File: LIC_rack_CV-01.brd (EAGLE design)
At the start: 162 x 102 mm, 53 parts, among them IC1 TS1117, IC2 MEGA32-A, IC3 MEGA8-AI, IC6 MAX481CSA, Q1 BSS138, Q2 14.7456, Q3 BSS138, Q4 14.7456, Q5 BSS138, Q6 BSS138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

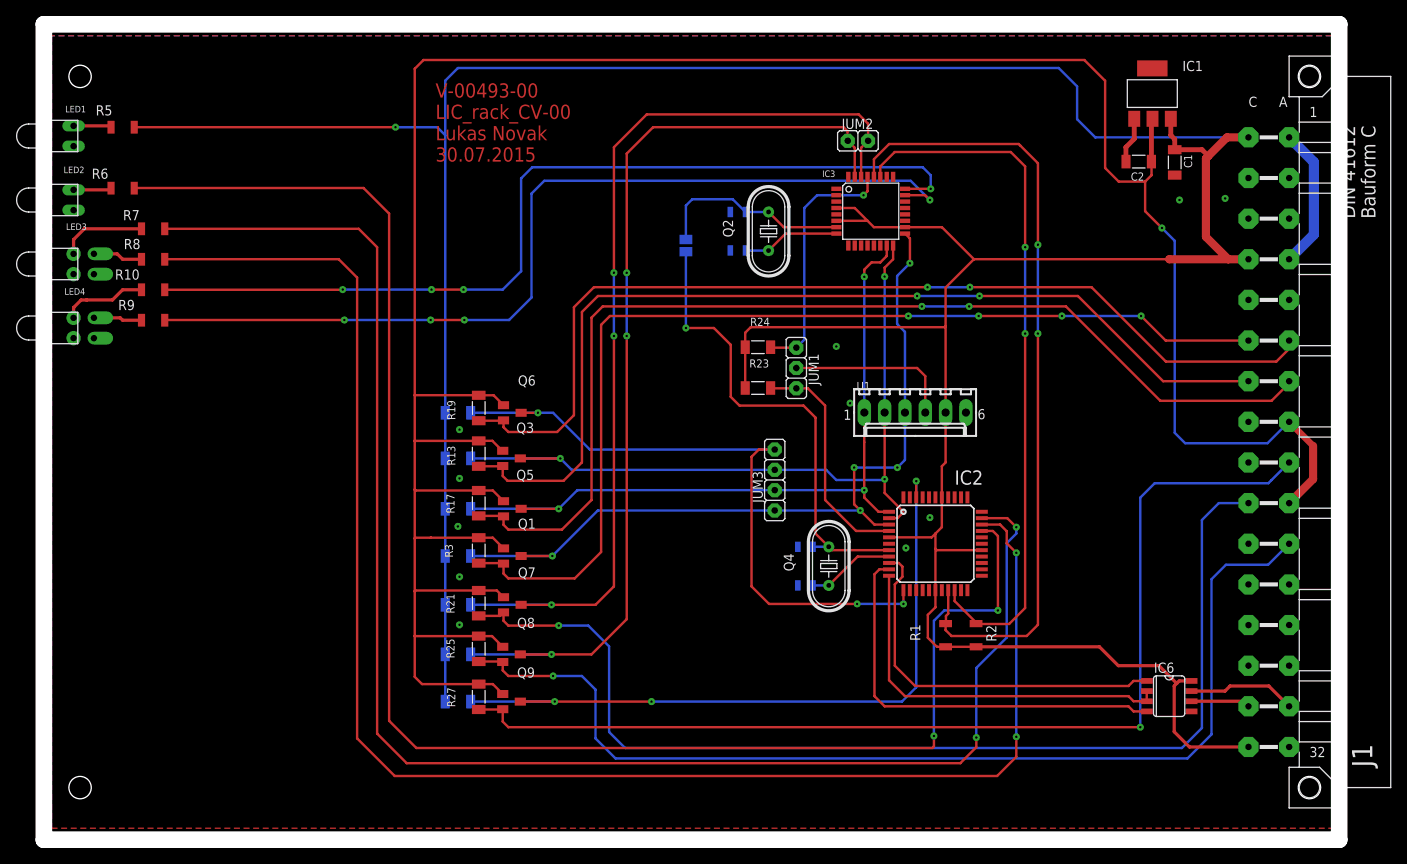
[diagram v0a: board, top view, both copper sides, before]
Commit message: Dalsi verze
Upravena deska skrz SS pin
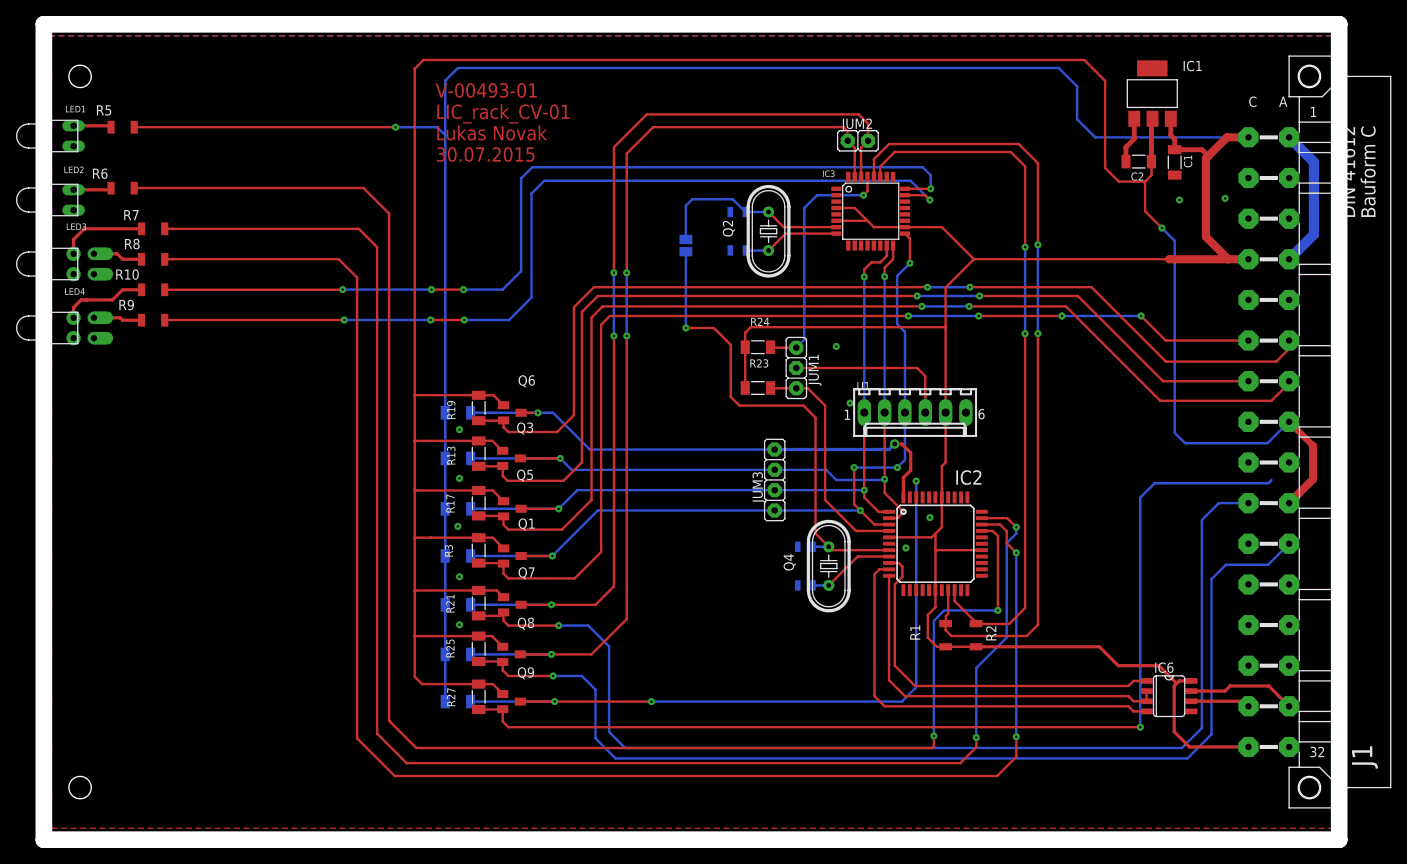
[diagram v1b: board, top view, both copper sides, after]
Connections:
- removed net N$4: IC2.44
- net PX_IRQ: no longer IC2.42
- net PX_IRQ_RFID: no longer J1.A18
- net PX_SS: now also IC2.44; no longer IC2.12
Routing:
- net PX_SS: track 83.1 -> 65.7 mm, vias 3 -> 2
- net PX_IRQ_RFID: track 133.7 -> 130.6 mm
- net PX_IRQ: track 88.5 -> 86.5 mm
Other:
- board text added: "V-00493-01 LIC_rack_CV-01 Lukas Novak 30.07.2015"
- board text removed: "V-00493-00 LIC_rack_CV-00 Lukas Novak 30.07.2015"
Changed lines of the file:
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@@
 <board>
 <plain>
-<text x="48" y="33.8" size="1.778" layer="1" font="vector" ratio="10">V-00493-00
-LIC_rack_CV-00
+<text x="48" y="33.8" size="1.778" layer="1" font="vector" ratio="10">V-00493-01
+LIC_rack_CV-01
 Lukas Novak
 30.07.2015</text>
@@
 </signal>
 <signal name="PX_SS">
-<contactref element="IC2" pad="12"/>
 <contactref element="Q6" pad="3"/>
 <contactref element="R20" pad="1"/>
 <contactref element="JUM3" pad="4"/>
-<wire x1="106.49" y1="-19.77" x2="106.49" y2="-21.49" width="0.3048" layer="1"/>
-<via x="106.49" y="-21.49" extent="1-16" drill="0.3"/>
-<wire x1="106.49" y1="-21.49" x2="100.7" y2="-21.49" width="0.3048" layer="16"/>
 <wire x1="58.7" y1="2.4" x2="60.8" y2="2.4" width="0.3048" layer="1"/>
 <via x="60.8" y="2.4" extent="1-16" drill="0.3"/>
@@
 <wire x1="67.3" y1="-2.2" x2="62.7" y2="2.4" width="0.3048" layer="16"/>
 <wire x1="62.7" y1="2.4" x2="60.8" y2="2.4" width="0.3048" layer="16"/>
-<wire x1="90.4" y1="-2.19" x2="88.41" y2="-2.19" width="0.3048" layer="1"/>
-<wire x1="88.41" y1="-2.19" x2="87.5" y2="-3.1" width="0.3048" layer="1"/>
-<wire x1="87.5" y1="-3.1" x2="87.5" y2="-19.3" width="0.3048" layer="1"/>
-<wire x1="87.5" y1="-19.3" x2="89.69" y2="-21.49" width="0.3048" layer="1"/>
-<wire x1="89.69" y1="-21.49" x2="100.7" y2="-21.49" width="0.3048" layer="1"/>
-<via x="100.7" y="-21.49" extent="1-16" drill="0.3"/>
+<contactref element="IC2" pad="44"/>
+<wire x1="90.4" y1="-2.19" x2="104.71" y2="-2.19" width="0.4064" layer="16"/>
+<wire x1="104.71" y1="-2.19" x2="105.4" y2="-1.5" width="0.4064" layer="16"/>
+<via x="105.4" y="-1.5" extent="1-16" drill="0.6"/>
+<wire x1="105.4" y1="-1.5" x2="106.3" y2="-1.5" width="0.4064" layer="1"/>
+<wire x1="106.3" y1="-1.5" x2="107.4" y2="-2.6" width="0.4064" layer="1"/>
+<wire x1="106.49" y1="-8.17" x2="106.49" y2="-5.71" width="0.4064" layer="1"/>
+<wire x1="106.49" y1="-5.71" x2="107.4" y2="-4.8" width="0.4064" layer="1"/>
+<wire x1="107.4" y1="-4.8" x2="107.4" y2="-2.6" width="0.4064" layer="1"/>
 </signal>
 <signal name="PX_SS_RFID">
@@
 </signal>
 <signal name="PX_IRQ_RFID">
-<contactref element="J1" pad="A18"/>
 <contactref element="R27" pad="1"/>
 <contactref element="Q9" pad="2"/>
@@
 <wire x1="56.4" y1="-34.65" x2="56.4" y2="-36.2" width="0.3048" layer="1"/>
 <wire x1="56.4" y1="-36.2" x2="57.1" y2="-36.9" width="0.3048" layer="1"/>
-<wire x1="154.7" y1="-3.81" x2="154.69" y2="-3.81" width="0.3048" layer="1"/>
 <wire x1="57.1" y1="-36.9" x2="136.1" y2="-36.9" width="0.3048" layer="1"/>
 <via x="136.1" y="-36.9" extent="1-16" drill="0.3"/>
 <wire x1="136.1" y1="-36.9" x2="136.1" y2="-8.2" width="0.3048" layer="16"/>
 <wire x1="136.1" y1="-8.2" x2="137.9" y2="-6.4" width="0.3048" layer="16"/>
-<wire x1="152.505" y1="-6.005" x2="154.7" y2="-3.81" width="0.3048" layer="16"/>
 <wire x1="137.9" y1="-6.4" x2="152.11" y2="-6.4" width="0.3048" layer="16"/>
 <wire x1="152.11" y1="-6.4" x2="152.505" y2="-6.005" width="0.3048" layer="16"/>
@@
 <via x="62.9" y="-33.7" extent="1-16" drill="0.3"/>
 <wire x1="62.9" y1="-33.7" x2="58.6" y2="-33.7" width="0.3048" layer="1"/>
-<contactref element="IC2" pad="42"/>
-<wire x1="108.09" y1="-8.17" x2="108.09" y2="-6.14" width="0.3048" layer="1"/>
 <via x="108.09" y="-6.14" extent="1-16" drill="0.3"/>
 <wire x1="108.09" y1="-6.14" x2="108.09" y2="-31.91" width="0.3048" layer="16"/>
@@
 <wire x1="58.7" y1="20.1" x2="58.7" y2="31.7" width="0.3048" layer="16"/>
 </signal>
-<signal name="N$4">
-<contactref element="IC2" pad="44"/>
-</signal>
 </signals>
